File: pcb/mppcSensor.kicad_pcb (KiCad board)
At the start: 2 copper layers, 13.6 x 4.5 mm, 3 parts, among them J1 Conn_Coaxial

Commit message: Removed old files updated libraries
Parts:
- added FD1: Fiducial, tooling:Fiducial_1.5mm_Mask3mm, F.Cu at (0.00, 0.00)
- D1: footprint s13360-2050ve:S13360-2050VE -> S13360-2050VE:S13360-2050VE
- H1: value MountingHole -> M1.6; footprint MountingHole:MountingHole_2.2mm_M2_ISO14580_Pad -> M1.6:M1.6; moved to B.Cu
- J1: value Conn_Coaxial -> U.FL; footprint Connector_Coaxial:U.FL_Hirose_U.FL-R-SMT-1_Vertical -> U.FL:U.FL
- turned H1 to 180 degrees
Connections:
- D1 pad 1: Net-(D1-Pad1) -> (no net)
- D1 pad 2: Net-(D1-Pad2) -> (no net)
- J1 pad 1: Net-(D1-Pad1) -> Net-(D1-PadA)
- J1 pad 2: Net-(D1-Pad2) -> Net-(D1-PadK)
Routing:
- net Net-(D1-PadK): track 0.00 -> 3.05 mm, vias 0 -> 2
- net Net-(D1-Pad2): track 3.05 -> 0.00 mm, vias 2 -> 0
- net Net-(D1-PadA): track 0.00 -> 1.65 mm, vias 0 -> 1
- net Net-(D1-Pad1): track 1.65 -> 0.00 mm, vias 1 -> 0
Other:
- net class Default removed

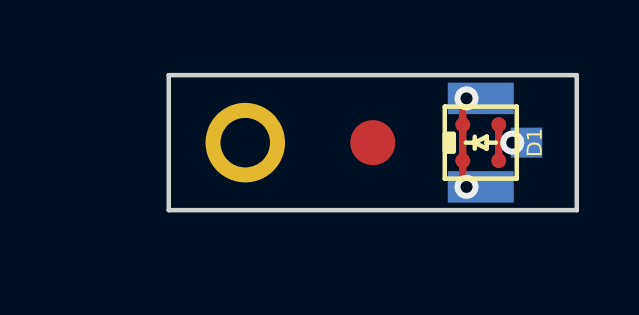
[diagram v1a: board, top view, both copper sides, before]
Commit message: Modified board to oshpark req .25x.25
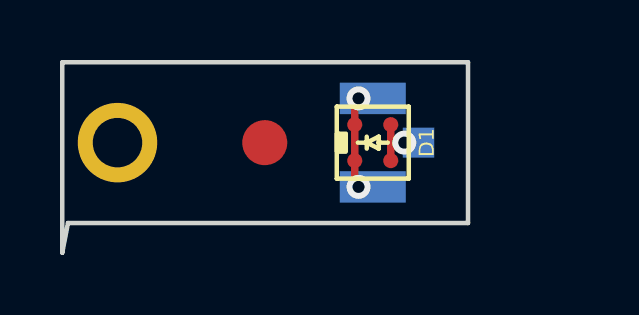
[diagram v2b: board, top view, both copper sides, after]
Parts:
- moved H1 4.26 mm to (-8.51, 0.00)
- moved D1 3.60 mm to (0.00, 0.00)
- moved FD1 3.60 mm to (-3.60, 0.00)
- moved J1 3.60 mm to (0.00, 0.00)
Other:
- board size 13.6 x 4.5 mm -> 13.5 x 6.3 mm
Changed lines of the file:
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@@
   (net 2 "Net-(D1-PadA)")
   (footprint "S13360-2050VE:S13360-2050VE" (layer "F.Cu")
-    (at 3.6 0 -90)
+    (at 0 0 -90)
     (descr "MPPC")
     (property "Sheetfile" "File: mppcSensor.kicad_sch")
     (property "Sheetname" "")
     (attr smd)
-    (fp_text reference "D1" (at 0 -1.8 -90) (layer "F.SilkS")
+    (fp_text reference "D1" (at 0 -1.8 90) (layer "F.SilkS")
       (effects (font (size 0.5 0.5) (thickness 0.1)))
     )
-    (fp_text value "S13360-2050VE" (at 0 2.5 -90) (layer "Eco2.User") hide
+    (fp_text value "S13360-2050VE" (at 0 2.5 90) (layer "Eco2.User") hide
       (effects (font (size 1 1) (thickness 0.15)))
     )
-    (fp_text user "${REFERENCE}" (at 0 0 -90) (layer "F.Fab")
+    (fp_text user "${REFERENCE}" (at 0 0 90) (layer "F.Fab")
       (effects (font (size 1 1) (thickness 0.15)))
     )
@@
   )
   (footprint "tooling:Fiducial_1.5mm_Mask3mm" (layer "F.Cu")
-    (at 0 0)
+    (at -3.6 0)
     (descr "Circular Fiducial, 1.5mm bare copper, 3mm soldermask opening")
     (tags "fiducial")
@@
   )
   (footprint "M1.6:M1.6" (layer "B.Cu")
-    (at -4.25 0 180)
+    (at -8.509 0 180)
     (descr "M1.6 Mounting Hole with 0.05mm clearence")
     (property "Sheetfile" "File: mppcSensor.kicad_sch")
@@
   )
   (footprint "U.FL:U.FL" (layer "B.Cu")
-    (at 3.6 0 180)
+    (at 0 0 180)
     (descr "Hirose U.FL Coaxial")
     (tags "Hirose U.FL Coaxial")
@@
     )
   )
-  (gr_line (start -6.8 -2.25) (end -6.8 2.25) (layer "Edge.Cuts") (width 0.15))
-  (gr_line (start -6.8 2.25) (end 6.8 2.25) (layer "Edge.Cuts") (width 0.15))
-  (gr_line (start 6.8 2.25) (end 6.8 -2.25) (layer "Edge.Cuts") (width 0.15))
-  (gr_line (start 6.8 -2.25) (end -6.8 -2.25) (layer "Edge.Cuts") (width 0.15))
+  (gr_line (start -10.3505 -2.6797) (end -10.3505 3.6703) (layer "Edge.Cuts") (width 0.15))
+  (gr_line (start -10.16 2.6797) (end -10.3505 3.6703) (layer "Edge.Cuts") (width 0.15))
+  (gr_line (start -10.16 2.6797) (end 3.175 2.6797) (layer "Edge.Cuts") (width 0.15))
+  (gr_line (start 3.175 2.6797) (end 3.175 -2.6797) (layer "Edge.Cuts") (width 0.15))
+  (gr_line (start 3.175 -2.6797) (end -10.3505 -2.6797) (layer "Edge.Cuts") (width 0.15))
   (gr_text "D1\nH1\nH2" (at -8.255 6.35) (layer "F.Fab")
     (effects (font (size 1 1) (thickness 0.2)))
   )
-  (segment (start 3 1.35) (end 3.125 1.475) (width 0.25) (layer "F.Cu") (net 1))
-  (segment (start 3 0.6) (end 3 1.35) (width 0.25) (layer "F.Cu") (net 1))
-  (segment (start 3 -1.35) (end 3.125 -1.475) (width 0.25) (layer "F.Cu") (net 1))
-  (segment (start 3 -0.6) (end 3 -1.35) (width 0.25) (layer "F.Cu") (net 1))
-  (segment (start 3 0.6) (end 3 -0.6) (width 0.25) (layer "F.Cu") (net 1))
-  (via (at 3.125 -1.475) (size 0.8) (drill 0.4) (layers "F.Cu" "B.Cu") (net 1))
-  (via (at 3.125 1.475) (size 0.8) (drill 0.4) (layers "F.Cu" "B.Cu") (net 1))
-  (segment (start 4.2 -0.6) (end 4.2 0) (width 0.25) (layer "F.Cu") (net 2))
-  (segment (start 4.2 0) (end 4.65 0) (width 0.25) (layer "F.Cu") (net 2))
-  (segment (start 4.2 0) (end 4.2 0.6) (width 0.25) (layer "F.Cu") (net 2))
-  (via (at 4.65 0) (size 0.8) (drill 0.4) (layers "F.Cu" "B.Cu") (net 2))
+  (segment (start -0.6 1.35) (end -0.475 1.475) (width 0.25) (layer "F.Cu") (net 1))
+  (segment (start -0.6 0.6) (end -0.6 1.35) (width 0.25) (layer "F.Cu") (net 1))
+  (segment (start -0.6 -1.35) (end -0.475 -1.475) (width 0.25) (layer "F.Cu") (net 1))
+  (segment (start -0.6 -0.6) (end -0.6 -1.35) (width 0.25) (layer "F.Cu") (net 1))
+  (segment (start -0.6 0.6) (end -0.6 -0.6) (width 0.25) (layer "F.Cu") (net 1))
+  (via (at -0.475 -1.475) (size 0.8) (drill 0.4) (layers "F.Cu" "B.Cu") (net 1))
+  (via (at -0.475 1.475) (size 0.8) (drill 0.4) (layers "F.Cu" "B.Cu") (net 1))
+  (segment (start 0.6 -0.6) (end 0.6 0) (width 0.25) (layer "F.Cu") (net 2))
+  (segment (start 0.6 0) (end 1.05 0) (width 0.25) (layer "F.Cu") (net 2))
+  (segment (start 0.6 0) (end 0.6 0.6) (width 0.25) (layer "F.Cu") (net 2))
+  (via (at 1.05 0) (size 0.8) (drill 0.4) (layers "F.Cu" "B.Cu") (net 2))
 )
